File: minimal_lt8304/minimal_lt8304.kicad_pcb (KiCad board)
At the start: 4 copper layers, 50.8 x 29.2 mm, 27 parts, among them J1 FW-02-03-G-D-085-155, J2 FW-02-03-G-D-085-155, T1 750315836, U1 LT8304IS8E-PBF

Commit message: Update project
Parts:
- added C8: 4.7 nF, capacitor_footprints:C_1210_140_3225Metric, F.Cu at (166.5, 121.1)
- added J3: FW-02-03-G-D-085-155, connector_footprints:FW-02-03-G-D-085-155, F.Cu at (186.0, 127.9)
- added J4: FW-02-03-G-D-085-155, connector_footprints:FW-02-03-G-D-085-155, F.Cu at (144.1, 127.9)
- added MB3: mouse-bite-midle-50mil-200mil, mouse_bite_footprints:mouse-bite-midle-50mil-200mil, F.Cu at (186.0, 124.8)
- added MB4: mouse-bite-midle-50mil-200mil, mouse_bite_footprints:mouse-bite-midle-50mil-200mil, F.Cu at (144.1, 124.8)
- added TP5: TestPoint, test_point_footprints:TestPoint_THTPad_Castelated, F.Cu at (186.6, 124.1)
- added TP6: TestPoint, test_point_footprints:TestPoint_THTPad_Castelated, F.Cu at (185.4, 124.1)
- added TP7: TestPoint, test_point_footprints:TestPoint_THTPad_Castelated, F.Cu at (143.5, 124.1)
- added TP8: TestPoint, test_point_footprints:TestPoint_THTPad_Castelated, F.Cu at (144.7, 124.1)
- moved TP1 0.64 mm to (144.7, 100.0)
- moved TP2 0.64 mm to (143.5, 100.0)
- moved TP3 0.64 mm to (185.4, 100.0)
- moved TP4 0.64 mm to (186.6, 100.0)
- moved J1 0.63 mm to (186.0, 96.2)
- moved J2 0.63 mm to (144.1, 96.2)
- moved MB1 0.63 mm to (144.1, 99.4)
- moved MB2 0.63 mm to (186.0, 99.4)
- moved C6 0.48 mm to (182.9, 107.4)
- moved C7 0.48 mm to (182.9, 116.7)
- moved C5 0.25 mm to (176.3, 102.2)
- moved R7 0.25 mm to (173.1, 102.2)
- moved D3 0.25 mm to (174.7, 104.3)
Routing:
- net GNDA: vias 55 -> 72
- net GND: vias 55 -> 72
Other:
- board size 50.8 x 29.2 mm -> 50.8 x 36.8 mm

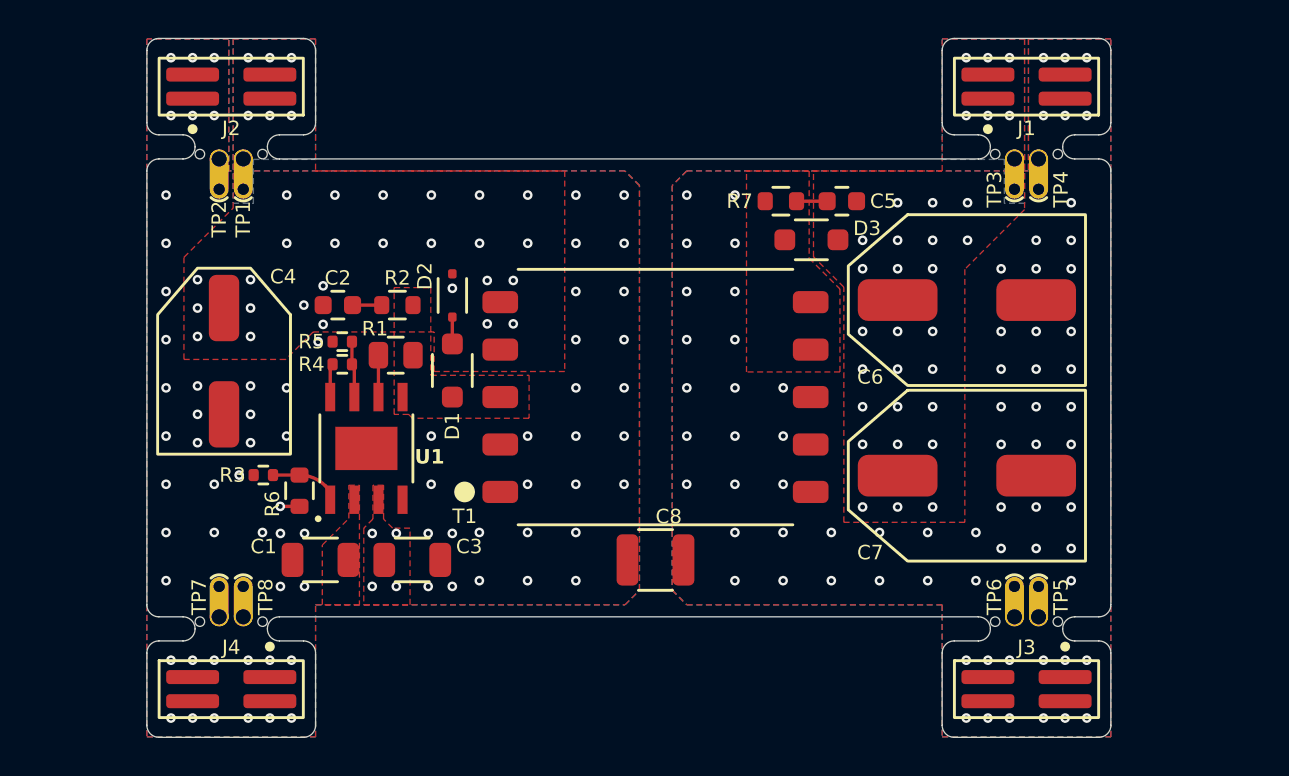
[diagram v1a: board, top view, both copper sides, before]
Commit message: Update ibom configuration to include additional component blacklist
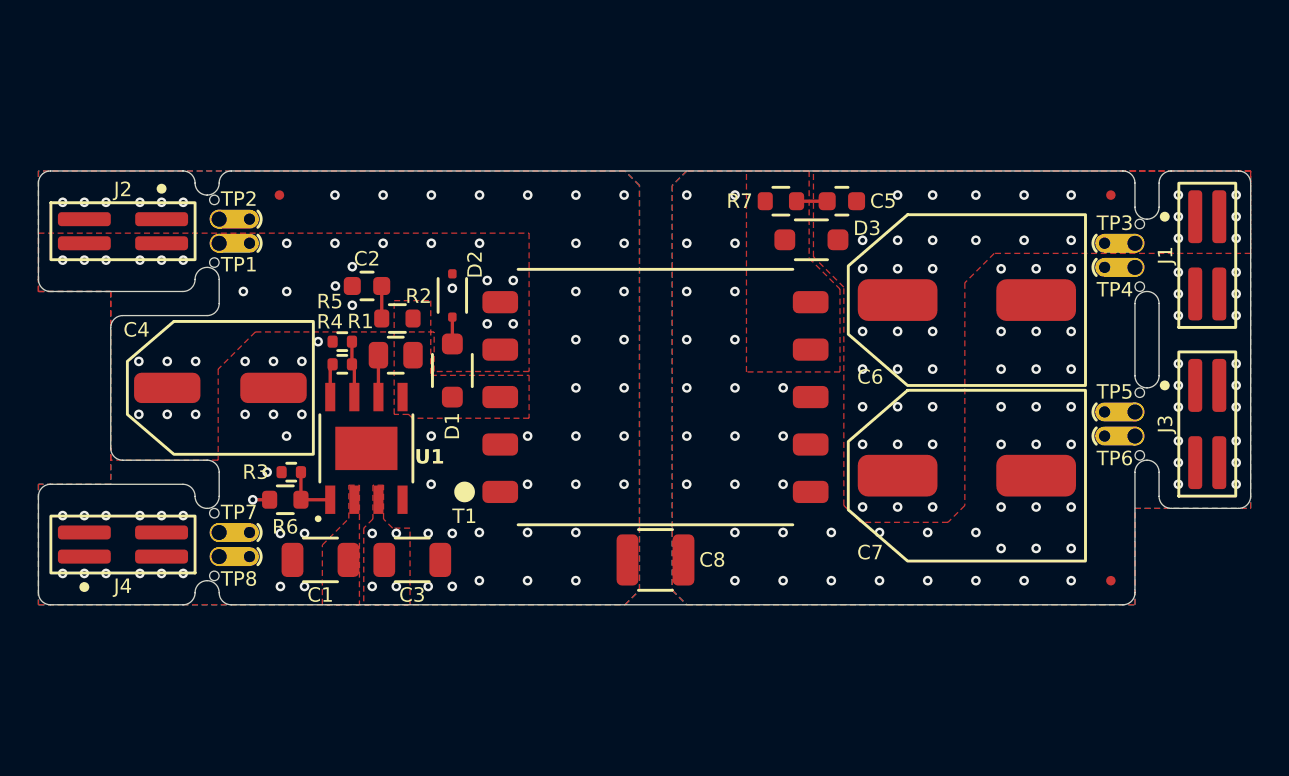
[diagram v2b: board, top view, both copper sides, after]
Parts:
- added FID1: Fiducial, no_components_footprints:Fiducial_0.5mm_Mask1mm, F.Cu at (190.4, 101.9)
- added FID2: Fiducial, no_components_footprints:Fiducial_0.5mm_Mask1mm, F.Cu at (146.6, 101.9)
- added FID3: Fiducial, no_components_footprints:Fiducial_0.5mm_Mask1mm, F.Cu at (190.4, 122.2)
- moved J3 16.9 mm to (195.5, 114.0), turned to 0 degrees
- moved J1 13.0 mm to (195.5, 105.1), turned to 0 degrees
- moved MB3 12.5 mm to (192.4, 114.0), turned to -90 degrees
- moved TP5 11.9 mm to (191.7, 113.3), turned to 180 degrees
- moved TP6 11.4 mm to (191.7, 114.6), turned to 180 degrees
- moved J4 9.52 mm to (138.4, 120.3), turned to 90 degrees
- moved J2 9.52 mm to (138.4, 103.8), turned to -90 degrees
- moved MB2 8.54 mm to (192.4, 105.1), turned to -90 degrees
- moved TP3 7.75 mm to (191.7, 104.4), turned to 180 degrees
- moved TP4 7.65 mm to (191.7, 105.7), turned to 180 degrees
- moved TP1 4.62 mm to (143.5, 104.4), turned to 0 degrees
- moved MB1 4.62 mm to (142.8, 103.8), turned to 90 degrees
- moved MB4 4.62 mm to (142.8, 120.3), turned to 90 degrees
- moved TP7 4.44 mm to (143.5, 119.7), turned to 0 degrees
- moved TP8 3.42 mm to (143.5, 121.0), turned to 0 degrees
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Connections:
- J2 pad 2: /VIN -> GND
- J2 pad 3: GND -> /VIN
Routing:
- net /EN/UVLO: track 3.72 -> 3.00 mm
- net /VIN: track 1.02 -> 0.89 mm, vias 37 -> 32
- net GNDA: vias 72 -> 70
- net GND: vias 72 -> 64
- net /VOUT: vias 31 -> 35
- removed copper zone on B.Cu, net /VIN
- removed copper zone on In2.Cu, net /VIN
- removed copper zone on B.Cu, net /VOUT
- removed copper zone on In2.Cu, net /VOUT
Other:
- board size 50.8 x 36.8 mm -> 63.9 x 22.9 mm
